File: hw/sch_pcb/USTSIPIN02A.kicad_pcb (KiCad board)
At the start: 4 copper layers, 90.9 x 50.3 mm, 151 parts, among them J1 SM08B-GHS-TB, J2 SD_Card-FPS009-4200-0, J22 HEADER_2x03, J3 SM06B-GHS-TB, J4 USBC_USB4105-GF-A, J5 HEADER_1x01, J6 HEADER_1x01, M1 HOLE, M2 HOLE, M3 HOLE, M4 HOLE, M8 BMI-S-204-F, Q1 2SK2394-6, Q2 BC817-25, Q3 BC817-25, Q4 BC817-25, U1 OPA2314, U10 ATMEGA1284P-AU, U11 PCF85263A, U12 MIC5504-3.3YM5, U2 OPA2314, U3 ISL21080DIH312Z-TK 1V25, U4 TS7211, U5 TS5A4594, U6 AT24CS64-SSHM, U7 USBLC6-2SC6, U8 TPS613222ADBV, U9 FT231XQ, Y1 16MHz, Y2 ABS07-120-32.768KHZ-T

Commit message: Edit PCB
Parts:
- moved R21 11.8 mm to (53.8, -18.3), turned to 180 degrees
- moved R20 10.8 mm to (53.8, -16.5), turned to 180 degrees
- moved C49 2.70 mm to (64.5, -23.6), turned to 180 degrees
- moved C51 2.59 mm to (65.8, -20.8)
- moved C60 2.59 mm to (65.0, -29.2), turned to -90 degrees
- moved R17 1.52 mm to (52.3, -32.0)
- moved C48 1.30 mm to (79.2, -18.0), turned to -90 degrees
- moved C39 1.27 mm to (54.6, -45.5), turned to 90 degrees
- moved U9 0.51 mm to (74.7, -17.3)
- moved C25 0.25 mm to (50.8, -25.4)
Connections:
- R28 pad 2: /power/RXLED/CBUS1 -> /power/TXLED/CBUS2
- R29 pad 2: /power/TXLED/CBUS2 -> /power/RXLED/CBUS1
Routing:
- net +3V3: track 6.00 -> 149.4 mm, vias 0 -> 5
- net /cpu/PC0: track 0.00 -> 70.0 mm, vias 0 -> 4
- net /cpu/PC1: track 0.00 -> 68.6 mm, vias 0 -> 5
- net POWER_ANALOG_3V3: track 59.9 -> 125.5 mm, vias 2 -> 8
- net +5V: track 0.00 -> 56.3 mm, vias 0 -> 3
- net TX0: track 0.00 -> 56.3 mm, vias 0 -> 3
- net RX0: track 0.00 -> 54.8 mm, vias 0 -> 2
- net /cpu/TIMEPULSE: track 0.00 -> 53.2 mm, vias 0 -> 4
- net Net-(BT1-Pad1): track 0.00 -> 51.2 mm, vias 0 -> 1
- net Vin: track 0.00 -> 44.4 mm, vias 0 -> 3
- net /cpu/EXTINT: track 0.00 -> 44.4 mm, vias 0 -> 2
- net /cpu/RX1: track 0.00 -> 43.9 mm, vias 0 -> 2
- net /cpu/TX1: track 0.00 -> 39.7 mm, vias 0 -> 2
- net /cpu/PC5_D1: track 0.00 -> 38.9 mm, vias 0 -> 2
- net RST#: track 0.00 -> 38.7 mm, vias 0 -> 2
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- added copper zone on In1.Cu, net GND
- added copper zone on In2.Cu, net GND

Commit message: Edit PCB
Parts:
- moved R31 9.40 mm to (87.6, -15.2), turned to 90 degrees
- moved R30 7.79 mm to (85.1, -15.2), turned to 90 degrees
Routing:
- net Net-(J4-PadB5): track 3.52 -> 12.4 mm
- net Net-(J4-PadA5): track 3.22 -> 8.95 mm
- net GND: track 74.1 -> 72.3 mm, vias 63 -> 282
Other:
- board text added: "2022"
- board text added: "USTSIPIN02A"
- board text removed: "2020"
- board text removed: "3V3"
- board text removed: "5V"
- board text removed: "GND"
- board text removed: "PC3"
- board text removed: "PC7"
- board text removed: "RST#"
- board text removed: "RX0"
- board text removed: "SPACEDOS01A_PCB01B"
- board text removed: "TX0"

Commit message: kontrola DRC
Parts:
- moved R14 1.12 mm to (13.3, -35.0)
- moved R41 0.73 mm to (13.2, -38.5)
- moved C37 0.47 mm to (17.1, -36.5)
- moved R12 0.46 mm to (24.8, -20.1)
- moved J2 0.16 mm to (91.0, -26.8)
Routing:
- net GND: track 72.3 -> 22.7 mm, vias 282 -> 283
- net Net-(C37-Pad1): track 5.44 -> 6.40 mm
- net +3V3: track 149.4 -> 148.5 mm
- net PB0: track 39.2 -> 40.0 mm
- net /K: track 5.40 -> 4.61 mm
- net RST#: track 38.7 -> 39.5 mm
- net +5V: track 56.3 -> 55.8 mm
- net (no net): vias 0 -> 1

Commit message: doreseni DRC
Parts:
- moved C32 159.3 mm to (179.2, 90.6)
- moved BT1 158.8 mm to (142.7, 78.9)
- moved C1 158.8 mm to (116.2, 106.1)
- moved C10 158.8 mm to (109.1, 100.5)
- moved C11 158.8 mm to (115.3, 101.1)
- moved C12 158.8 mm to (129.7, 102.6)
- moved C13 158.8 mm to (124.2, 108.2)
- moved C14 158.8 mm to (120.1, 108.5)
- moved C15 158.8 mm to (115.5, 96.7)
- moved C16 158.8 mm to (117.3, 96.7)
- moved C17 158.8 mm to (121.7, 96.1)
- moved C18 158.8 mm to (122.5, 98.9)
- moved C19 158.8 mm to (130.0, 93.0)
- moved C2 158.8 mm to (121.8, 89.9)
- moved C20 158.8 mm to (107.9, 107.4)
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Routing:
- net Vin: track 44.4 -> 43.4 mm
- net +3V3: track 148.5 -> 148.0 mm
- net (no net): vias 1 -> 0
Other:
- board text added: "PC3 PC4"
- board text added: "Prog."
- board text added: "ust.cz, 2022"

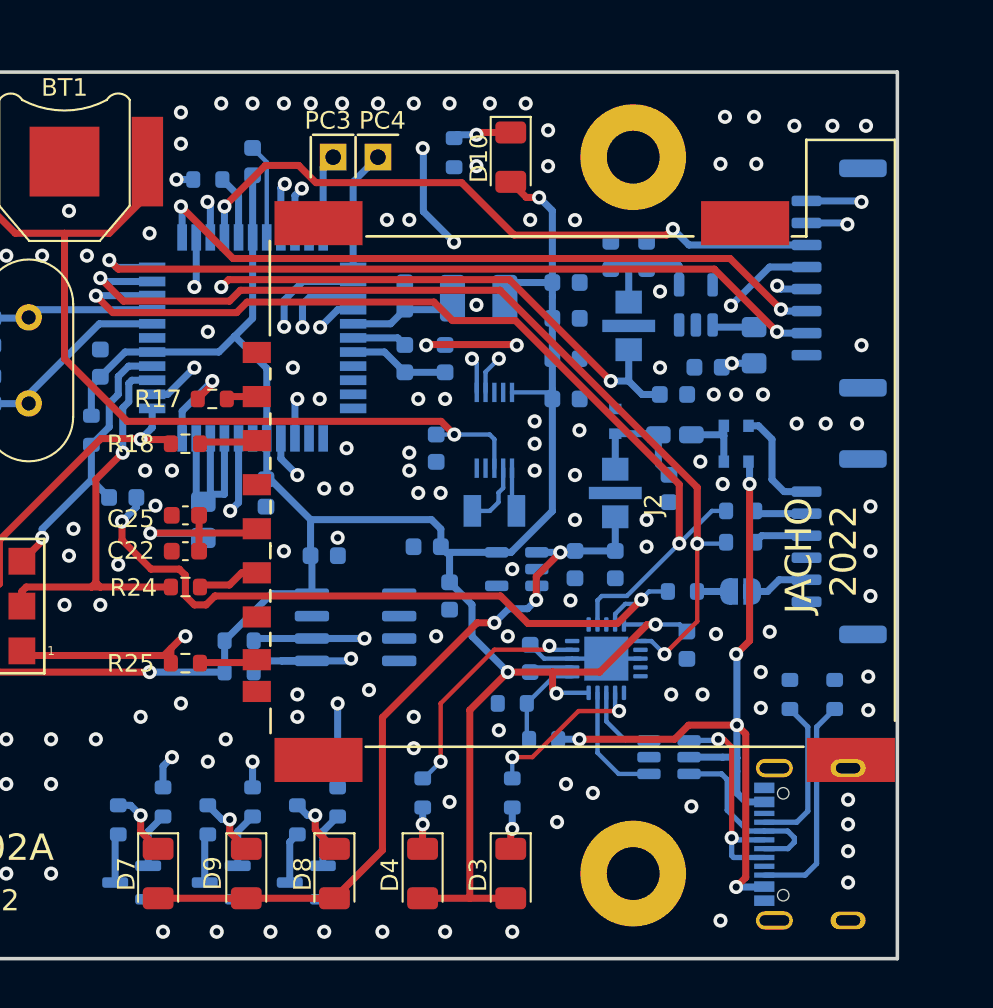
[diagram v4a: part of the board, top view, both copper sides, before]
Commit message: Edit schema and PCB
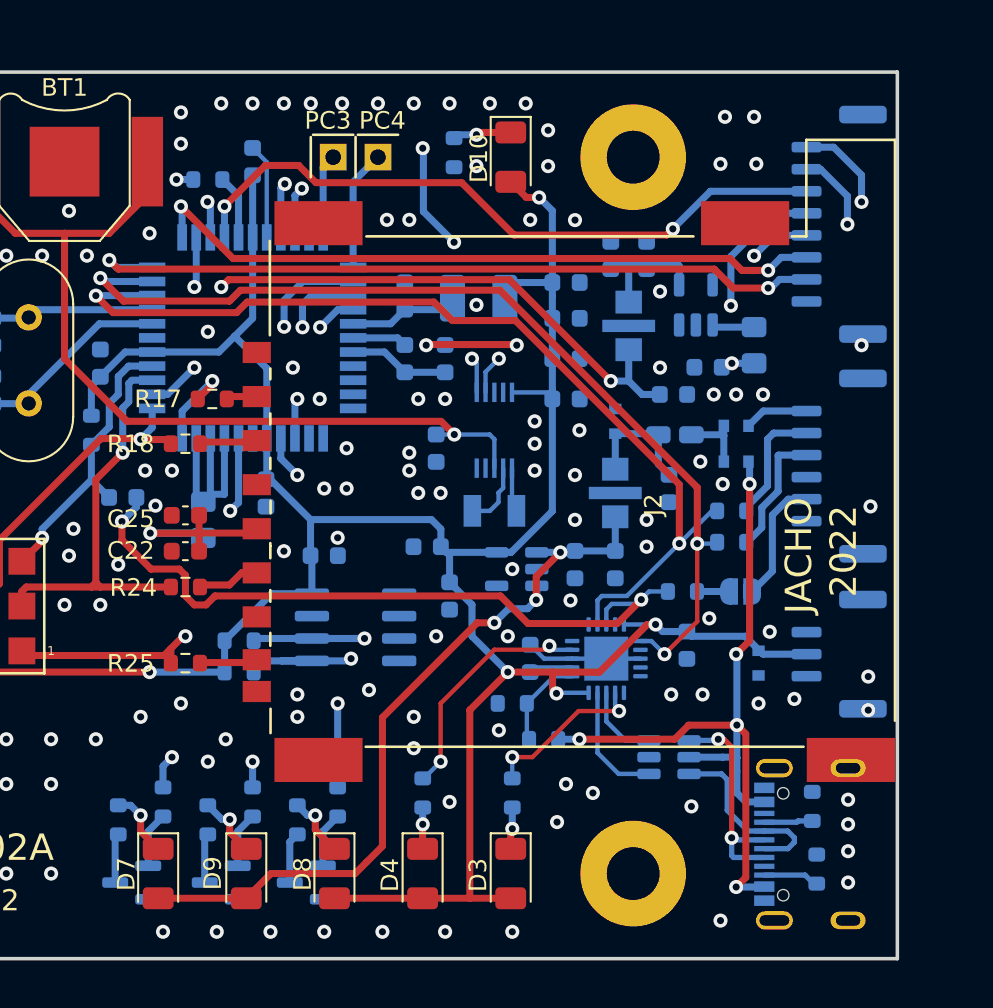
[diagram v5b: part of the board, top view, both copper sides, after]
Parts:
- added D11: BZX585-B5V6.115, Diode_SMD:D_SOD-523, B.Cu at (182.1, 107.4)
- added J7: SM03B-GHS-TB, Connector_JST:JST_GH_SM03B-GHS-TB_1x03-1MP_P1.25mm_Horizontal, B.Cu at (186.7, 106.9)
- moved R31 9.96 mm to (185.4, 119.1)
- moved R30 6.48 mm to (185.1, 115.5)
- moved J3 4.57 mm to (186.7, 96.2)
- moved J1 3.05 mm to (186.7, 82.5)
- moved R33 0.51 mm to (180.6, 98.7)
- moved R34 0.51 mm to (180.6, 100.5)
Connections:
- D8 pad 2: Vin -> +3V3
- U9 pad 18: unconnected-(U9-Pad18) -> RST#
- U9 pad 19: RST# -> unconnected-(U9-Pad19)
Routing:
- net +3V3: track 148.0 -> 160.3 mm
- net Net-(J4-PadB5): track 12.4 -> 3.18 mm
- net Net-(J4-PadA5): track 8.95 -> 2.75 mm
- net Net-(J3-Pad3): track 3.07 -> 7.32 mm
- net Net-(J3-Pad2): track 2.98 -> 6.92 mm
- net Net-(J3-Pad5): track 3.36 -> 7.13 mm
- net /cpu/PC1: track 68.6 -> 71.5 mm
- net /cpu/PC0: track 69.9 -> 72.5 mm
- net UAV_5V: track 6.18 -> 3.64 mm
- net /cpu/EXTINT: track 44.4 -> 46.8 mm
- net /cpu/TIMEPULSE: track 53.2 -> 55.4 mm
- net /cpu/RX1: track 43.9 -> 43.0 mm
- net RST#: track 40.0 -> 40.6 mm
- net /cpu/TX1: track 39.7 -> 39.1 mm
- net TX0: track 55.9 -> 55.4 mm
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
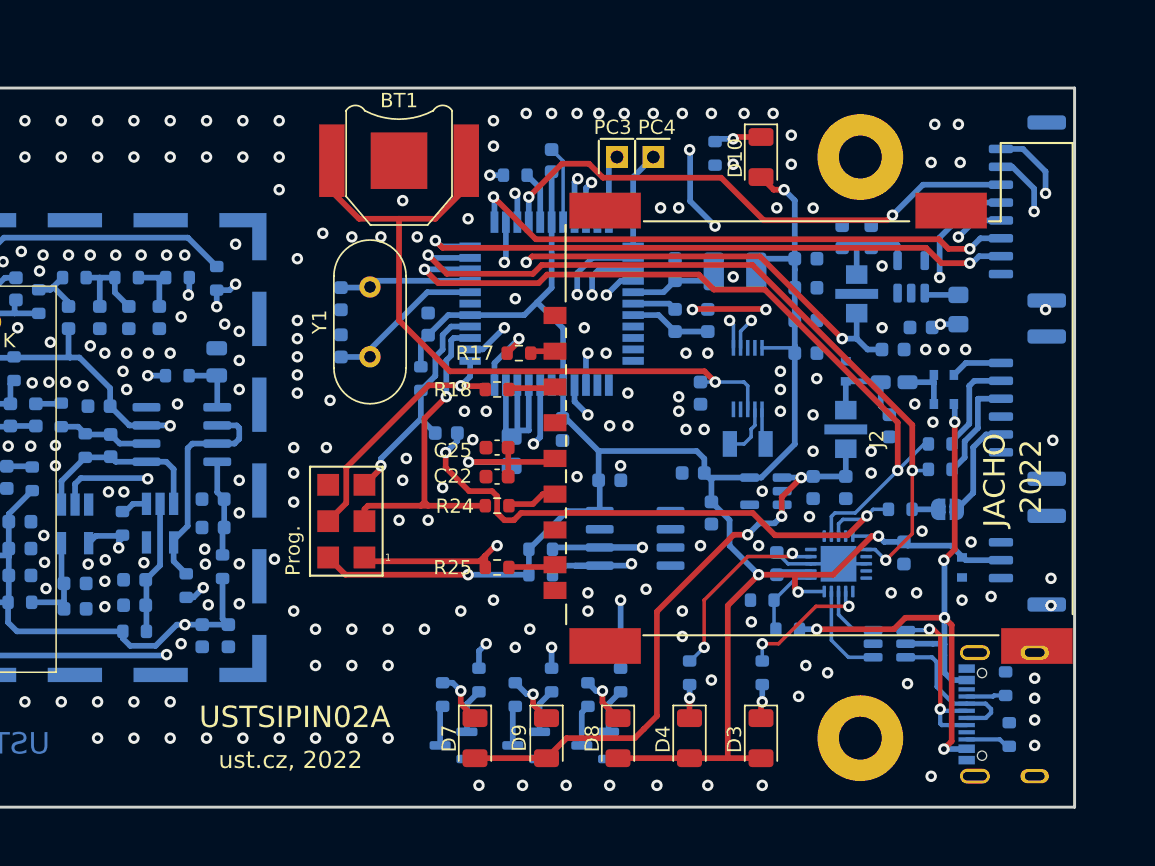
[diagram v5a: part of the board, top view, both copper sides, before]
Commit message: Edit schema and PCB
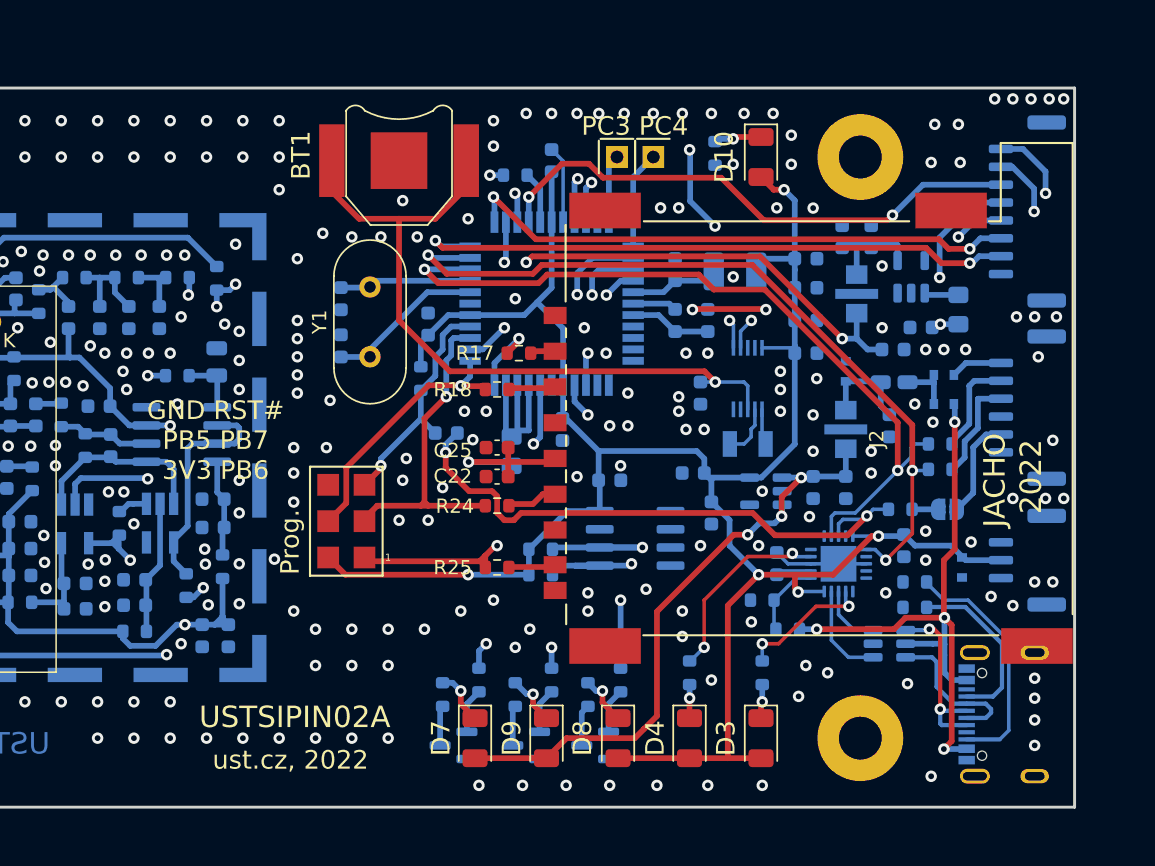
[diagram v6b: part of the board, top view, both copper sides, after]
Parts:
- moved R31 12.5 mm to (178.8, 108.4), turned to 180 degrees
- moved R30 8.29 mm to (178.8, 110.2), turned to 180 degrees
- moved C48 0.51 mm to (178.0, 105.9)
- moved R12 0.22 mm to (123.2, 104.3)
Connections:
- U8 pad 3: (no net) -> unconnected-(U8-Pad3)
- U8 pad 5: (no net) -> unconnected-(U8-Pad5)
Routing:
- net Net-(J4-PadB5): track 3.18 -> 17.0 mm
- net Net-(J4-PadA5): track 2.75 -> 12.1 mm
- net POWER_ANALOG_3V3: track 125.1 -> 126.0 mm
- net GND: vias 275 -> 286
- net /power/VBUS: vias 5 -> 4
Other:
- board text added: "GND RST# PB5 PB7 3V3 PB6"

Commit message: Edit PCB
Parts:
- added G***: LOGO, MLAB_LOGA:UST, F.Cu at (135.4, 111.8)

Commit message: uprava silkscreenu, vycisteni repozitare
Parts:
- moved R17 1.53 mm to (149.6, 92.5)
- renumbered G*** to G1
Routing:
- net /cpu/PB4: track 5.32 -> 8.22 mm
- net Net-(D4-Pad1): track 2.35 -> 4.10 mm
- net Net-(D3-Pad1): track 2.38 -> 4.13 mm
- net Net-(J2-Pad1): track 1.76 -> 3.29 mm
- net Net-(D9-Pad1): track 3.64 -> 5.12 mm
- net Net-(D7-Pad1): track 3.82 -> 5.26 mm
- net Net-(D8-Pad1): track 3.61 -> 4.98 mm
- net Net-(D10-Pad1): track 3.35 -> 4.54 mm
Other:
- board text added: "GND PB5 3V3"
- board text added: "LED1"
- board text added: "LED2"
- board text added: "LED3"
- board text added: "PWR"
- board text added: "RST# PB7 PB6"
- board text added: "USB RX"
- board text added: "USB TX"
- board text removed: "GND RST# PB5 PB7 3V3 PB6"
